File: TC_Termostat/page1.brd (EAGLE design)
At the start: 30 parts, among them IC1 F20X3---N14, P1_1 SOLDER_POINTA, P1_2 SOLDER_POINTA, P1_4 SOLDER_POINTA, P1_5 SOLDER_POINTA, P1_6 SOLDER_POINTA, P1_7 SOLDER_POINTA, P2_7 SOLDER_POINTA, Q1 2N2219A, X1 J_PROG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

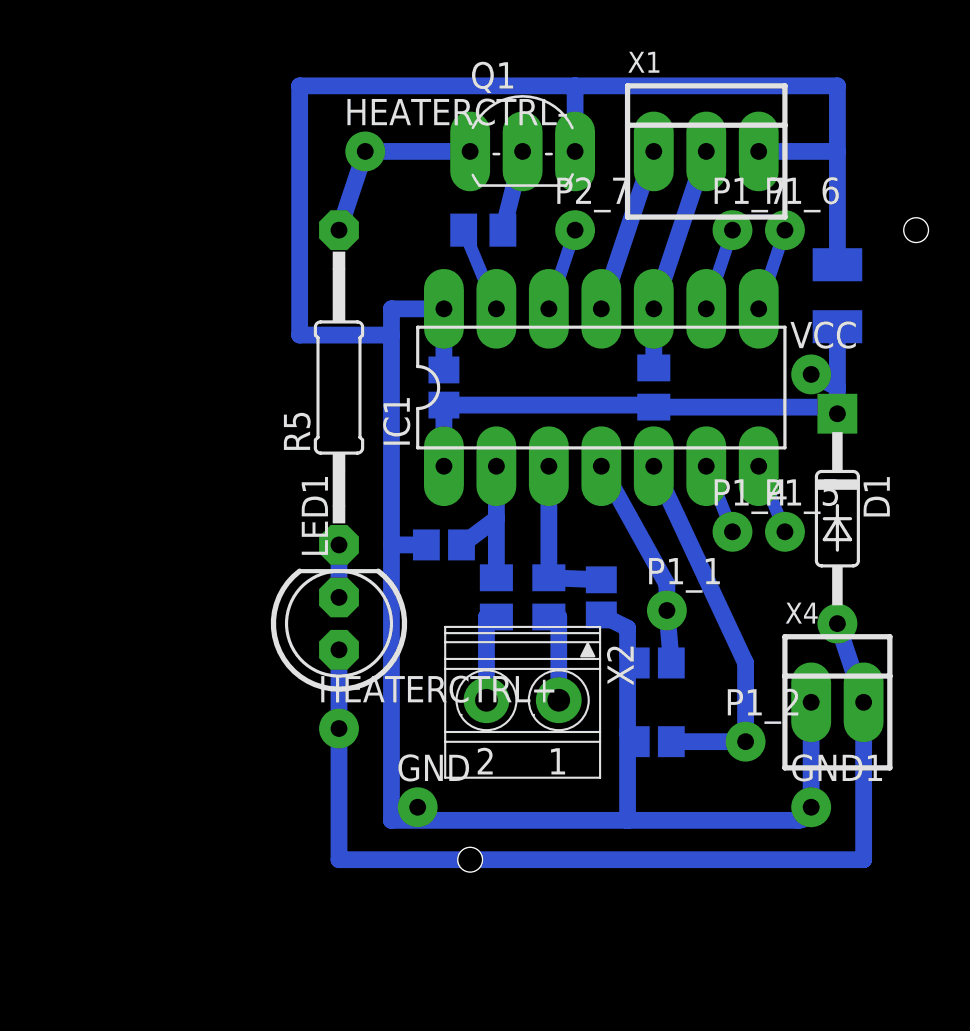
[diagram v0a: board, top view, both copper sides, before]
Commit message: Added revised Schematic  for TC-Thermostat
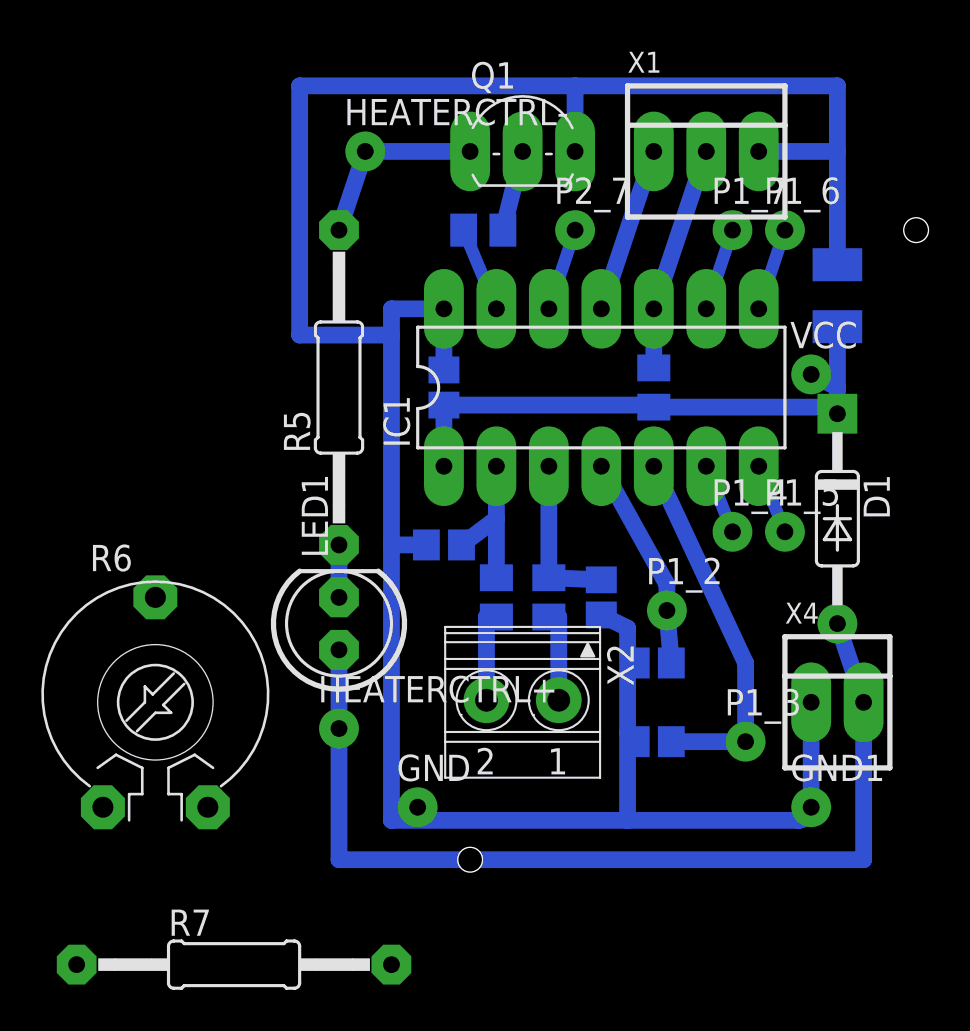
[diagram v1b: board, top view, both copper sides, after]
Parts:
- removed P1_1: SOLDER_POINTA, Stofer:P1-13
- added P1_3: SOLDER_POINTA, Stofer:P1-13
- added R6: 5k, rcl:PT-10
- added R7: 5k, rcl:0207/15
- R4: value 29K -> 12k
- R5: value 32 O -> 330O
- moved P1_2 7.41 mm to (22.2, 13.3)
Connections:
- net N$7: now also P1_3.1; no longer P1_2.1
- net N$9: now also P1_2.1; no longer P1_1.1
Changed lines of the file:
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@@
 <grid distance="0.05" unitdist="inch" unit="inch" style="lines" multiple="1" display="no" altdistance="0.025" altunitdist="inch" altunit="inch"/>
 <layers>
-<layer number="1" name="Top" color="4" fill="1" visible="no" active="yes"/>
+<layer number="1" name="Top" color="4" fill="1" visible="yes" active="yes"/>
 <layer number="2" name="Route2" color="1" fill="3" visible="no" active="no"/>
 <layer number="3" name="Route3" color="4" fill="3" visible="no" active="no"/>
@@
 <layer number="18" name="Vias" color="2" fill="1" visible="yes" active="yes"/>
 <layer number="19" name="Unrouted" color="6" fill="1" visible="yes" active="yes"/>
-<layer number="20" name="Dimension" color="15" fill="1" visible="no" active="yes"/>
-<layer number="21" name="tPlace" color="7" fill="1" visible="no" active="yes"/>
-<layer number="22" name="bPlace" color="7" fill="1" visible="no" active="yes"/>
-<layer number="23" name="tOrigins" color="15" fill="1" visible="no" active="yes"/>
-<layer number="24" name="bOrigins" color="15" fill="1" visible="no" active="yes"/>
+<layer number="20" name="Dimension" color="15" fill="1" visible="yes" active="yes"/>
+<layer number="21" name="tPlace" color="7" fill="1" visible="yes" active="yes"/>
+<layer number="22" name="bPlace" color="7" fill="1" visible="yes" active="yes"/>
+<layer number="23" name="tOrigins" color="15" fill="1" visible="yes" active="yes"/>
+<layer number="24" name="bOrigins" color="15" fill="1" visible="yes" active="yes"/>
 <layer number="25" name="tNames" color="7" fill="1" visible="no" active="yes"/>
 <layer number="26" name="bNames" color="7" fill="1" visible="no" active="yes"/>
@@
 <element name="X4" library="con-molex" package="22-23-2021" value="PWR" x="30.48" y="8.89"/>
 <element name="Q1" library="transistor-npn" package="TO92-EBC" value="2N2219A" x="15.24" y="36.83"/>
-<element name="R4" library="rcl" package="M0805" value="29K" x="13.335" y="31.75" rot="MR0"/>
+<element name="R4" library="rcl" package="M0805" value="12k" x="13.335" y="31.75" rot="MR0"/>
 <element name="HEATERCTRL-" library="Stofer" package="P1-13" value="SOLDER_POINTA" x="7.62" y="35.56"/>
 <element name="HEATERCTRL+" library="Stofer" package="P1-13" value="SOLDER_POINTA" x="6.35" y="7.62"/>
 <element name="LED1" library="led" package="LED5MM" value="" x="6.35" y="12.7" rot="R90"/>
-<element name="R5" library="rcl" package="0207/15" value="32 O" x="6.35" y="24.13" rot="R90"/>
+<element name="R5" library="rcl" package="0207/15" value="330O" x="6.35" y="24.13" rot="R90"/>
 <element name="P1_5" library="Stofer" package="P1-13" value="SOLDER_POINTA" x="27.94" y="17.145"/>
 <element name="P1_4" library="Stofer" package="P1-13" value="SOLDER_POINTA" x="25.4" y="17.145"/>
@@
 <element name="D1" library="dedenbear" package="DIO-35-10" value="1N4148" x="30.48" y="17.78" rot="R270"/>
 <element name="C5" library="rcl" package="C0805" value="1uf" x="11.43" y="16.51" rot="MR0"/>
-<element name="P1_1" library="Stofer" package="P1-13" value="SOLDER_POINTA" x="22.225" y="13.335"/>
-<element name="P1_2" library="Stofer" package="P1-13" value="SOLDER_POINTA" x="26.035" y="6.985"/>
+<element name="P1_2" library="Stofer" package="P1-13" value="SOLDER_POINTA" x="22.225" y="13.335"/>
+<element name="P1_3" library="Stofer" package="P1-13" value="SOLDER_POINTA" x="26.035" y="6.985"/>
 <element name="C6" library="rcl" package="C0805" value="1uf" x="19.05" y="13.97" rot="MR270"/>
 <element name="X2" library="con-phoenix-350" package="1751248" value="1751248" x="15.24" y="8.89" rot="R180">
@@
 <attribute name="OC_FARNELL" value="unknown" x="15.24" y="8.89" size="1.778" layer="27" rot="R180" display="off"/>
 </element>
+<element name="R6" library="rcl" package="PT-10" value="5k" x="-2.54" y="8.89"/>
+<element name="R7" library="rcl" package="0207/15" value="5k" x="1.27" y="-3.81"/>
 </elements>
 <signals>
@@
 <contactref element="IC1" pad="5"/>
 <contactref element="C2" pad="1"/>
-<contactref element="P1_2" pad="1"/>
+<contactref element="P1_3" pad="1"/>
 <wire x1="21.59" y1="20.32" x2="26.035" y2="10.795" width="0.8128" layer="16"/>
 <wire x1="26.035" y1="10.795" x2="26.035" y2="6.985" width="0.8128" layer="16"/>
@@
 <contactref element="C1" pad="1"/>
 <contactref element="IC1" pad="4"/>
-<contactref element="P1_1" pad="1"/>
+<contactref element="P1_2" pad="1"/>
 <wire x1="19.05" y1="20.32" x2="22.225" y2="14.605" width="0.8128" layer="16"/>
 <wire x1="22.225" y1="14.605" x2="22.225" y2="13.335" width="0.8128" layer="16"/>
@@
 </signal>
 </signals>
-<errors>
-</errors>
 </board>
 </drawing>
